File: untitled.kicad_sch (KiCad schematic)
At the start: 12 parts, among them U2 LM76005

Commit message: cleaned up file structure
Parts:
- renumbered Cboot to Cboot1, Cin to Cin1, Cinx to Cinx1, Cout to Cout1, Coutx to Coutx1, Cvcc to Cvcc1, Rfbb to Rfbb1, Rfbt to Rfbt1, Rpgood to Rpgood1

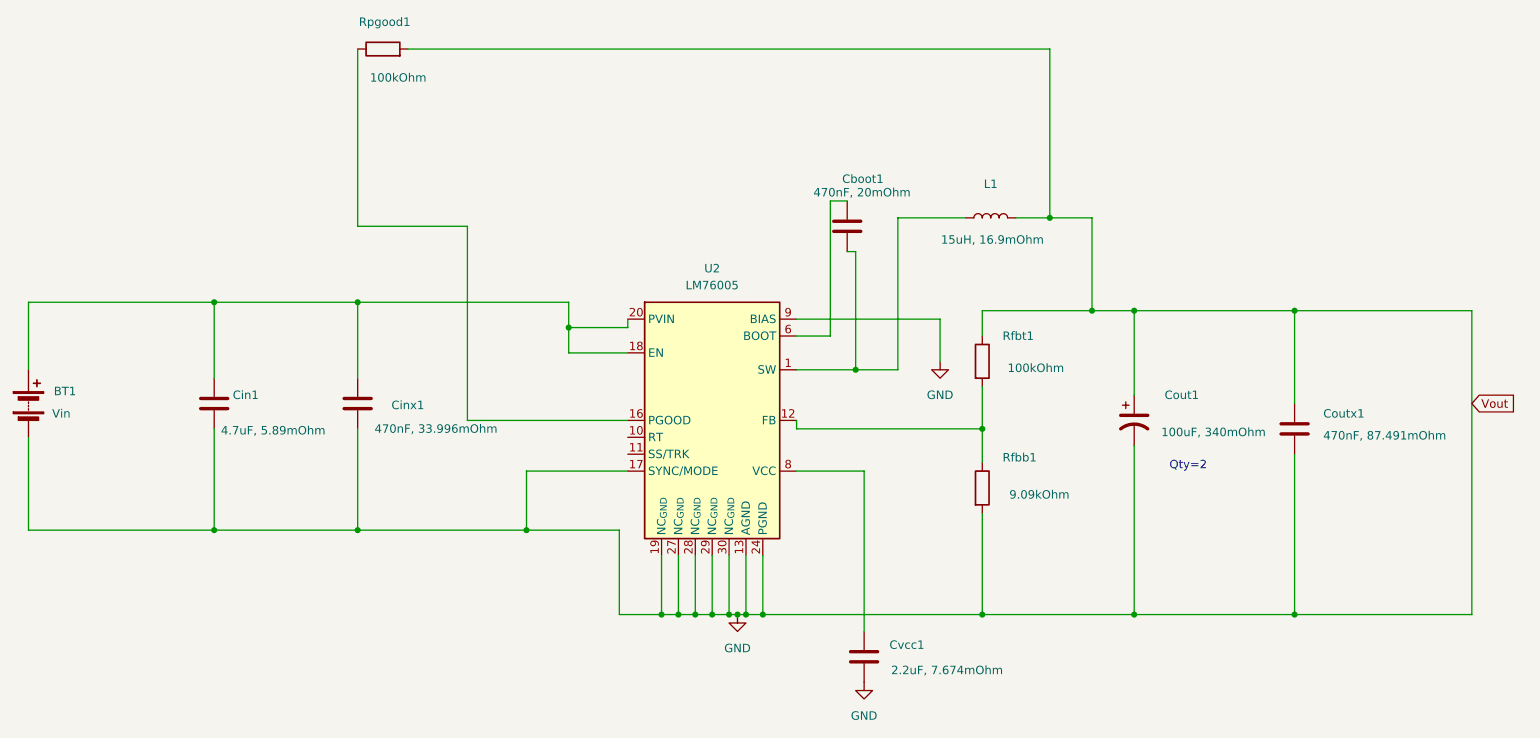
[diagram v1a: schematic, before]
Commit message: feat: 48-5v buck converter
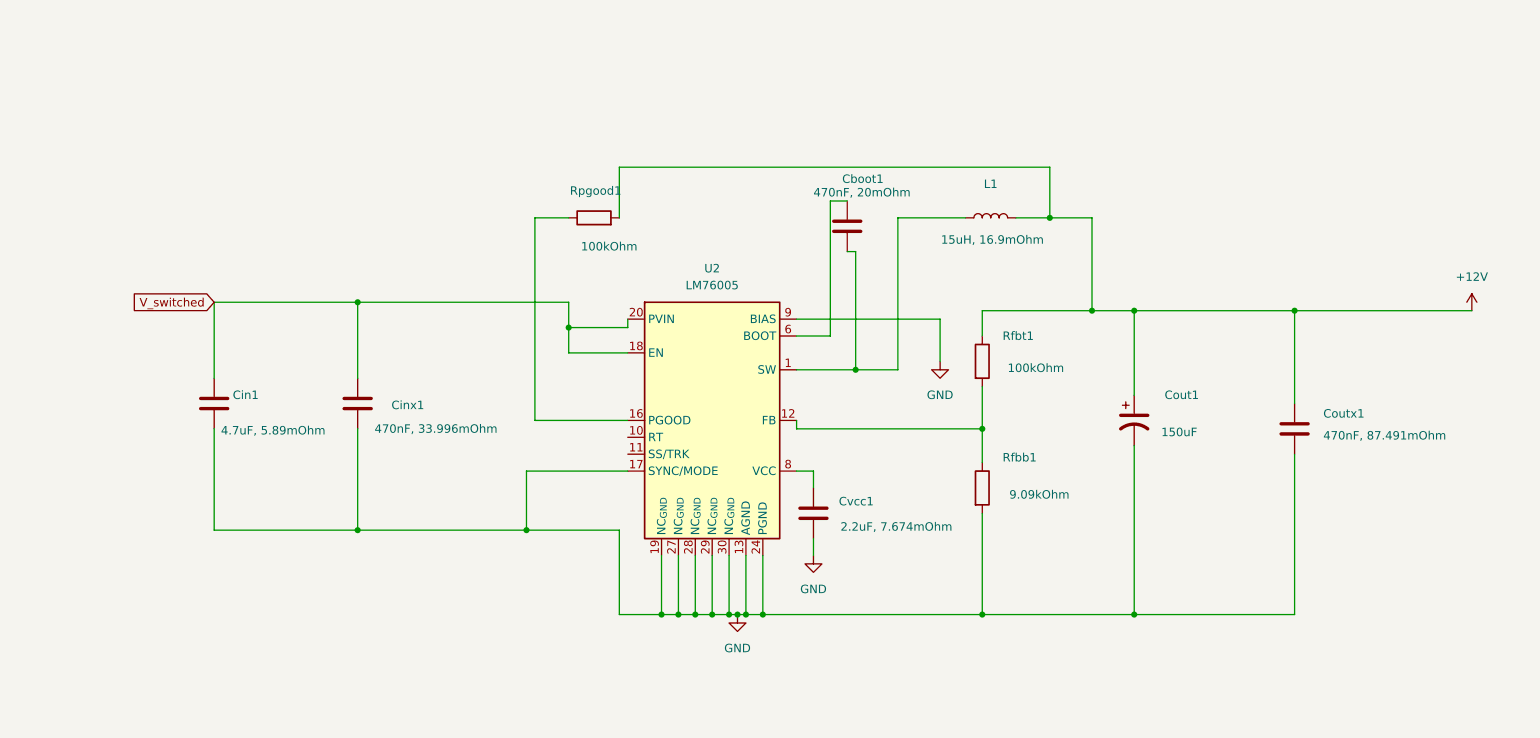
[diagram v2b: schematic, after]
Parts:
- removed BT1: Vin, symbol Device:Battery
- Cboot1, Cin1, Cinx1, Coutx1, Cvcc1: footprint Capacitor_SMD:CP_Elec_3x5.3 -> Capacitor_SMD:C_0805_2012Metric_Pad1.18x1.45mm_HandSolder
- Cout1: value 100uF, 340mOhm -> 150uF; footprint (none) -> Capacitor_SMD:C_0805_2012Metric_Pad1.18x1.45mm_HandSolder
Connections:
- net GND: no longer Cout1.1, Coutx1.1, L1.2, Rfbt1.1, Rpgood1.2
- net V_switched: now reaches Cin1.1, Cinx1.1, U2.18 (EN), U2.20 (PVIN), U2.21 (PVIN), U2.22 (PVIN)
- new net +12V: Cout1.1, Coutx1.1, L1.2, Rfbt1.1, Rpgood1.2
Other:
- note removed: "Qty=2"
- company: (none) -> UMass Robotics
- title: (none) -> 48 to 12v Buck Converter
- moved on the sheet: Cvcc1, Rpgood1

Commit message: Fixed ERC
Created Buck3
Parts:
- removed Cboot1: 470nF, 20mOhm, Capacitor_SMD:C_0805_2012Metric_Pad1.18x1.45mm_HandSolder, symbol Device:C
- removed Cin1: 4.7uF, 5.89mOhm, Capacitor_SMD:C_0805_2012Metric_Pad1.18x1.45mm_HandSolder, symbol Device:C
- removed Cinx1: 470nF, 33.996mOhm, Capacitor_SMD:C_0805_2012Metric_Pad1.18x1.45mm_HandSolder, symbol Device:C
- removed Cout1: 150uF, Capacitor_SMD:C_0805_2012Metric_Pad1.18x1.45mm_HandSolder, symbol Device:C_Polarized_US
- removed Coutx1: 470nF, 87.491mOhm, Capacitor_SMD:C_0805_2012Metric_Pad1.18x1.45mm_HandSolder, symbol Device:C
- removed Cvcc1: 2.2uF, 7.674mOhm, Capacitor_SMD:C_0805_2012Metric_Pad1.18x1.45mm_HandSolder, symbol Device:C
- removed L1: 15uH, 16.9mOhm, Inductor_SMD:L_6.3x6.3_H3, symbol Device:L
- removed Rfbb1: 9.09kOhm, Resistor_SMD:R_0201_0603Metric, symbol Device:R
- removed Rfbt1, Rpgood1: 100kOhm, Resistor_SMD:R_0201_0603Metric, symbol Device:R
- removed U2: LM76005, Package_DFN_QFN:Texas_RNP0030B_WQFN-30-1EP_4x6mm_P0.5mm_EP1.8x4.5mm_ThermalVias, symbol Regulator_Switching:LM76005

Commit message: Cleaned up repo, fixing naming
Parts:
- added Cboot?: 470nF, 20mOhm, Capacitor_SMD:C_0805_2012Metric_Pad1.18x1.45mm_HandSolder, symbol Device:C
- added Cin?: 4.7uF, 5.89mOhm, Capacitor_SMD:C_0805_2012Metric_Pad1.18x1.45mm_HandSolder, symbol Device:C
- added Cinx?: 470nF, 33.996mOhm, Capacitor_SMD:C_0805_2012Metric_Pad1.18x1.45mm_HandSolder, symbol Device:C
- added Cout?: 150uF, Capacitor_SMD:C_0805_2012Metric_Pad1.18x1.45mm_HandSolder, symbol Device:C_Polarized_US
- added Coutx?: 470nF, 87.491mOhm, Capacitor_SMD:C_0805_2012Metric_Pad1.18x1.45mm_HandSolder, symbol Device:C
- added Cvcc?: 2.2uF, 7.674mOhm, Capacitor_SMD:C_0805_2012Metric_Pad1.18x1.45mm_HandSolder, symbol Device:C
- added L?: 15uH, 16.9mOhm, Inductor_SMD:L_6.3x6.3_H3, symbol Device:L
- added Rfbb?: 9.09kOhm, Resistor_SMD:R_0201_0603Metric, symbol Device:R
- added Rfbt?, Rpgood?: 100kOhm, Resistor_SMD:R_0201_0603Metric, symbol Device:R
- added U?: LM76005, Package_DFN_QFN:Texas_RNP0030B_WQFN-30-1EP_4x6mm_P0.5mm_EP1.8x4.5mm_ThermalVias, symbol Regulator_Switching:LM76005
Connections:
- new net: Cboot?.1, U?.6 (BOOT)
- new net: Cboot?.2, L?.1, U?.1 (SW), U?.2 (SW), U?.3 (SW), U?.4 (SW), U?.5 (SW)
- new net: Cvcc?.1, U?.8 (VCC)
- new net: Rpgood?.1, U?.16 (PGOOD)
- new net: Rfbb?.1, Rfbt?.2, U?.12 (FB)
- new net +12V: Cout?.1, Coutx?.1, L?.2, Rfbt?.1, Rpgood?.2
- new net GND: Cin?.2, Cinx?.2, Cout?.2, Coutx?.2, Cvcc?.2, Rfbb?.2, U?.13 (AGND), U?.14 (AGND), U?.15 (AGND), U?.17 (SYNC/MODE), U?.19 (NC_{GND}), U?.24 (PGND), U?.25 (PGND), U?.26 (PGND), U?.27 (NC_{GND}), U?.28 (NC_{GND}), U?.29 (NC_{GND}), U?.30 (NC_{GND}), U?.31 (AGND), U?.9 (BIAS)
- new net V_switched: Cin?.1, Cinx?.1, U?.18 (EN), U?.20 (PVIN), U?.21 (PVIN), U?.22 (PVIN)
